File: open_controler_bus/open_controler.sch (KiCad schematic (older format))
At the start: 4 parts, among them J1 Conn_02x20_Odd_Even, J2 Conn_02x20_Odd_Even, J3 Conn_02x20_Odd_Even, J4 Conn_02x20_Odd_Even

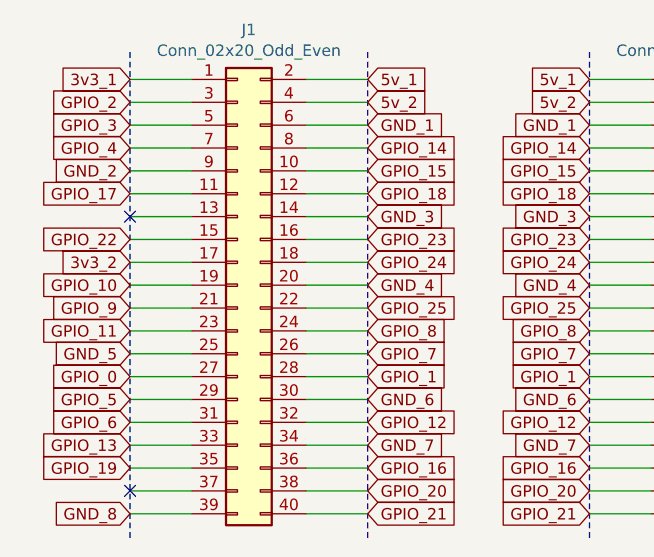
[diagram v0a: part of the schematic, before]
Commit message: 3d anadido a open controles bus
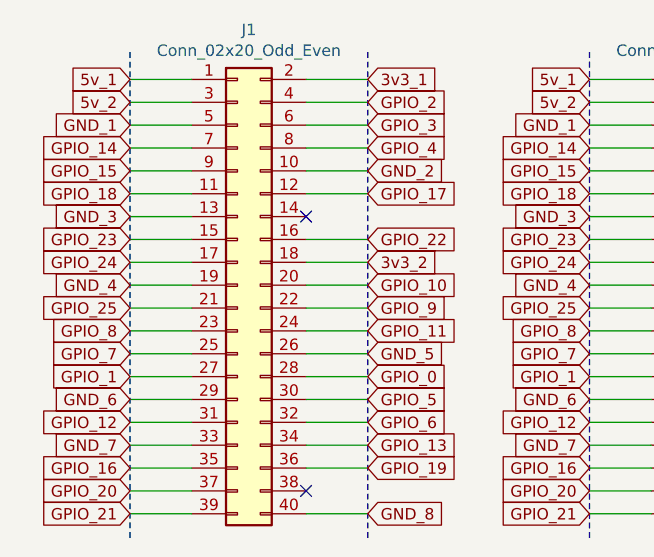
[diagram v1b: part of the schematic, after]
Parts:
- J1: footprint Connector_PinHeader_2.54mm:PinHeader_2x20_P2.54mm_Vertical -> Connector_PinSocket_2.54mm:PinSocket_2x20_P2.54mm_Horizontal
- J2, J3, J4: footprint Connector_PinHeader_2.54mm:PinHeader_2x20_P2.54mm_Vertical -> Connector_PinHeader_2.54mm:PinHeader_2x20_P2.54mm_Horizontal
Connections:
- net 3v3_1: now also J1.2 (Pin_2); no longer J1.1 (Pin_1)
- net 3v3_2: now also J1.18 (Pin_18); no longer J1.17 (Pin_17)
- net 5v_1: now also J1.1 (Pin_1); no longer J1.2 (Pin_2)
- net 5v_2: now also J1.3 (Pin_3); no longer J1.4 (Pin_4)
- net GND_1: now also J1.5 (Pin_5); no longer J1.6 (Pin_6)
- net GND_2: now also J1.10 (Pin_10); no longer J1.9 (Pin_9)
- net GND_3: now also J1.13 (Pin_13); no longer J1.14 (Pin_14)
- net GND_4: now also J1.19 (Pin_19); no longer J1.20 (Pin_20)
- net GND_5: now also J1.26 (Pin_26); no longer J1.25 (Pin_25)
- net GND_6: now also J1.29 (Pin_29); no longer J1.30 (Pin_30)
- net GND_7: now also J1.33 (Pin_33); no longer J1.34 (Pin_34)
- net GND_8: now also J1.40 (Pin_40); no longer J1.39 (Pin_39)
- net GPIO_0: now also J1.28 (Pin_28); no longer J1.27 (Pin_27)
- net GPIO_1: now also J1.27 (Pin_27); no longer J1.28 (Pin_28)
- net GPIO_10: now also J1.20 (Pin_20); no longer J1.19 (Pin_19)
- net GPIO_11: now also J1.24 (Pin_24); no longer J1.23 (Pin_23)
- net GPIO_12: now also J1.31 (Pin_31); no longer J1.32 (Pin_32)
- net GPIO_13: now also J1.34 (Pin_34); no longer J1.33 (Pin_33)
- net GPIO_14: now also J1.7 (Pin_7); no longer J1.8 (Pin_8)
- net GPIO_15: now also J1.9 (Pin_9); no longer J1.10 (Pin_10)
- net GPIO_16: now also J1.35 (Pin_35); no longer J1.36 (Pin_36)
- net GPIO_17: now also J1.12 (Pin_12); no longer J1.11 (Pin_11)
- net GPIO_18: now also J1.11 (Pin_11); no longer J1.12 (Pin_12)
- net GPIO_19: now also J1.36 (Pin_36); no longer J1.35 (Pin_35)
- net GPIO_2: now also J1.4 (Pin_4); no longer J1.3 (Pin_3)
- net GPIO_20: now also J1.37 (Pin_37); no longer J1.38 (Pin_38)
- net GPIO_21: now also J1.39 (Pin_39); no longer J1.40 (Pin_40)
- net GPIO_22: now also J1.16 (Pin_16); no longer J1.15 (Pin_15)
- net GPIO_23: now also J1.15 (Pin_15); no longer J1.16 (Pin_16)
- net GPIO_24: now also J1.17 (Pin_17); no longer J1.18 (Pin_18)
- net GPIO_25: now also J1.21 (Pin_21); no longer J1.22 (Pin_22)
- net GPIO_3: now also J1.6 (Pin_6); no longer J1.5 (Pin_5)
- net GPIO_4: now also J1.8 (Pin_8); no longer J1.7 (Pin_7)
- net GPIO_5: now also J1.30 (Pin_30); no longer J1.29 (Pin_29)
- net GPIO_6: now also J1.32 (Pin_32); no longer J1.31 (Pin_31)
- net GPIO_7: now also J1.25 (Pin_25); no longer J1.26 (Pin_26)
- net GPIO_8: now also J1.23 (Pin_23); no longer J1.24 (Pin_24)
- net GPIO_9: now also J1.22 (Pin_22); no longer J1.21 (Pin_21)
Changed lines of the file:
@@
 F 0 "J1" H 2330 3237 50  0000 C CNN
 F 1 "Conn_02x20_Odd_Even" H 2330 3146 50  0000 C CNN
-F 2 "Connector_PinHeader_2.54mm:PinHeader_2x20_P2.54mm_Vertical" H 2280 2120 50  0001 C CNN
+F 2 "Connector_PinSocket_2.54mm:PinSocket_2x20_P2.54mm_Horizontal" H 2280 2120 50  0001 C CNN
 F 3 "~" H 2280 2120 50  0001 C CNN
 	1    2280 2120
 	1    0    0    -1
 $EndComp
-Text GLabel 1810 1220 0    50   Input ~ 0
-3v3_1
 Wire Notes Line
 	1810 1100 1810 3230
-Text GLabel 1810 1320 0    50   Input ~ 0
-GPIO_2
-Text GLabel 1810 1420 0    50   Input ~ 0
-GPIO_3
-Text GLabel 1810 1520 0    50   Input ~ 0
-GPIO_4
-Text GLabel 1810 1620 0    50   Input ~ 0
-GND_2
-Text GLabel 1810 1720 0    50   Input ~ 0
-GPIO_17
-Text GLabel 1810 1920 0    50   Input ~ 0
-GPIO_22
-Text GLabel 1810 2020 0    50   Input ~ 0
-3v3_2
-Text GLabel 1810 2120 0    50   Input ~ 0
-GPIO_10
-Text GLabel 1810 2220 0    50   Input ~ 0
-GPIO_9
-Text GLabel 1810 2320 0    50   Input ~ 0
-GPIO_11
-Text GLabel 1810 2420 0    50   Input ~ 0
-GND_5
-Text GLabel 1810 2520 0    50   Input ~ 0
-GPIO_0
-Text GLabel 1810 2620 0    50   Input ~ 0
-GPIO_5
-Text GLabel 1810 2720 0    50   Input ~ 0
-GPIO_6
-Text GLabel 1810 2820 0    50   Input ~ 0
-GPIO_13
-Text GLabel 1810 2920 0    50   Input ~ 0
-GPIO_19
-Text GLabel 1810 3120 0    50   Input ~ 0
-GND_8
 Wire Wire Line
 	1810 1220 2080 1220
 Wire Notes Line
 	2850 1100 2850 3230
-Text GLabel 2850 1220 2    50   Input ~ 0
-5v_1
-Text GLabel 2850 1320 2    50   Input ~ 0
-5v_2
-Text GLabel 2850 1420 2    50   Input ~ 0
-GND_1
-Text GLabel 2850 1520 2    50   Input ~ 0
-GPIO_14
-Text GLabel 2850 1620 2    50   Input ~ 0
-GPIO_15
-Text GLabel 2850 1820 2    50   Input ~ 0
-GND_3
-Text GLabel 2850 1920 2    50   Input ~ 0
-GPIO_23
-Text GLabel 2850 2020 2    50   Input ~ 0
-GPIO_24
-Text GLabel 2850 2120 2    50   Input ~ 0
-GND_4
-Text GLabel 2850 2220 2    50   Input ~ 0
-GPIO_25
-Text GLabel 2850 2320 2    50   Input ~ 0
-GPIO_8
-Text GLabel 2850 2420 2    50   Input ~ 0
-GPIO_7
-Text GLabel 2850 2520 2    50   Input ~ 0
-GPIO_1
-Text GLabel 2850 2620 2    50   Input ~ 0
-GND_6
-Text GLabel 2850 2720 2    50   Input ~ 0
-GPIO_12
-Text GLabel 2850 2820 2    50   Input ~ 0
-GND_7
-Text GLabel 2850 2920 2    50   Input ~ 0
-GPIO_16
-Text GLabel 2850 3020 2    50   Input ~ 0
-GPIO_20
-Text GLabel 2850 3120 2    50   Input ~ 0
-GPIO_21
 Wire Wire Line
 	1810 1320 2080 1320
@@
 	2580 1720 2850 1720
 Wire Wire Line
-	2580 1820 2850 1820
-Wire Wire Line
 	2580 1920 2850 1920
 Wire Wire Line
@@
 Wire Wire Line
 	2580 2920 2850 2920
-Wire Wire Line
-	2580 3020 2850 3020
 Wire Wire Line
 	2580 3120 2850 3120
@@
 F 0 "J3" H 6350 3237 50  0000 C CNN
 F 1 "Conn_02x20_Odd_Even" H 6350 3146 50  0000 C CNN
-F 2 "Connector_PinHeader_2.54mm:PinHeader_2x20_P2.54mm_Vertical" H 6300 2120 50  0001 C CNN
+F 2 "Connector_PinHeader_2.54mm:PinHeader_2x20_P2.54mm_Horizontal" H 6300 2120 50  0001 C CNN
 F 3 "~" H 6300 2120 50  0001 C CNN
 	1    6300 2120
@@
 Wire Wire Line
 	6600 3120 6870 3120
-NoConn ~ 1810 1820
-NoConn ~ 1810 3020
 Wire Notes Line
 	6870 1100 6870 3230
-Text GLabel 2850 1720 2    50   Input ~ 0
-GPIO_18
 Wire Wire Line
 	6600 1720 6870 1720
@@
 F 0 "J2" H 4340 3237 50  0000 C CNN
 F 1 "Conn_02x20_Odd_Even" H 4340 3146 50  0000 C CNN
-F 2 "Connector_PinHeader_2.54mm:PinHeader_2x20_P2.54mm_Vertical" H 4290 2120 50  0001 C CNN
+F 2 "Connector_PinHeader_2.54mm:PinHeader_2x20_P2.54mm_Horizontal" H 4290 2120 50  0001 C CNN
 F 3 "~" H 4290 2120 50  0001 C CNN
 	1    4290 2120
@@
 F 0 "J4" H 8370 3237 50  0000 C CNN
 F 1 "Conn_02x20_Odd_Even" H 8370 3146 50  0000 C CNN
-F 2 "Connector_PinHeader_2.54mm:PinHeader_2x20_P2.54mm_Vertical" H 8320 2120 50  0001 C CNN
+F 2 "Connector_PinHeader_2.54mm:PinHeader_2x20_P2.54mm_Horizontal" H 8320 2120 50  0001 C CNN
 F 3 "~" H 8320 2120 50  0001 C CNN
 	1    8320 2120
@@
 Wire Wire Line
 	8620 1720 8890 1720
+Text GLabel 1810 1220 0    50   Input ~ 0
+5v_1
+Text GLabel 1810 1320 0    50   Input ~ 0
+5v_2
+Text GLabel 1810 1420 0    50   Input ~ 0
+GND_1
+Text GLabel 1810 1520 0    50   Input ~ 0
+GPIO_14
+Text GLabel 1810 1620 0    50   Input ~ 0
+GPIO_15
+Text GLabel 1810 1720 0    50   Input ~ 0
+GPIO_18
+Text GLabel 1810 1820 0    50   Input ~ 0
+GND_3
+Text GLabel 1810 1920 0    50   Input ~ 0
+GPIO_23
+Text GLabel 1810 2020 0    50   Input ~ 0
+GPIO_24
+Text GLabel 1810 2120 0    50   Input ~ 0
+GND_4
+Text GLabel 1810 2220 0    50   Input ~ 0
+GPIO_25
+Text GLabel 1810 2320 0    50   Input ~ 0
+GPIO_8
+Text GLabel 1810 2420 0    50   Input ~ 0
+GPIO_7
+Text GLabel 1810 2520 0    50   Input ~ 0
+GPIO_1
+Text GLabel 1810 2620 0    50   Input ~ 0
+GND_6
+Text GLabel 1810 2720 0    50   Input ~ 0
+GPIO_12
+Text GLabel 1810 2820 0    50   Input ~ 0
+GND_7
+Text GLabel 1810 2920 0    50   Input ~ 0
+GPIO_16
+Text GLabel 1810 3020 0    50   Input ~ 0
+GPIO_20
+Text GLabel 1810 3120 0    50   Input ~ 0
+GPIO_21
+Text GLabel 2850 1220 2    50   Input ~ 0
+3v3_1
+Text GLabel 2850 1320 2    50   Input ~ 0
+GPIO_2
+Text GLabel 2850 1420 2    50   Input ~ 0
+GPIO_3
+Text GLabel 2850 1520 2    50   Input ~ 0
+GPIO_4
+Text GLabel 2850 1620 2    50   Input ~ 0
+GND_2
+Text GLabel 2850 1720 2    50   Input ~ 0
+GPIO_17
+Text GLabel 2850 1920 2    50   Input ~ 0
+GPIO_22
+Text GLabel 2850 2020 2    50   Input ~ 0
+3v3_2
+Text GLabel 2850 2120 2    50   Input ~ 0
+GPIO_10
+Text GLabel 2850 2220 2    50   Input ~ 0
+GPIO_9
+Text GLabel 2850 2320 2    50   Input ~ 0
+GPIO_11
+Text GLabel 2850 2420 2    50   Input ~ 0
+GND_5
+Text GLabel 2850 2520 2    50   Input ~ 0
+GPIO_0
+Text GLabel 2850 2620 2    50   Input ~ 0
+GPIO_5
+Text GLabel 2850 2720 2    50   Input ~ 0
+GPIO_6
+Text GLabel 2850 2820 2    50   Input ~ 0
+GPIO_13
+Text GLabel 2850 2920 2    50   Input ~ 0
+GPIO_19
+Text GLabel 2850 3120 2    50   Input ~ 0
+GND_8
+NoConn ~ 2580 3020
+NoConn ~ 2580 1820
 $EndSCHEMATC
